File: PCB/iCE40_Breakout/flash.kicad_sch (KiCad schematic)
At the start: 47 parts, among them J4 prog_hdr, Q10 L2N7002SLLT1G, Q11 L2N7002SLLT1G, Q12 L2N7002SLLT1G, Q2 L2N7002SLLT1G, Q3 L2N7002SLLT1G, Q4 L2N7002SLLT1G, Q5 L2N7002SLLT1G, Q6 L2N7002SLLT1G, Q7 L2N7002SLLT1G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

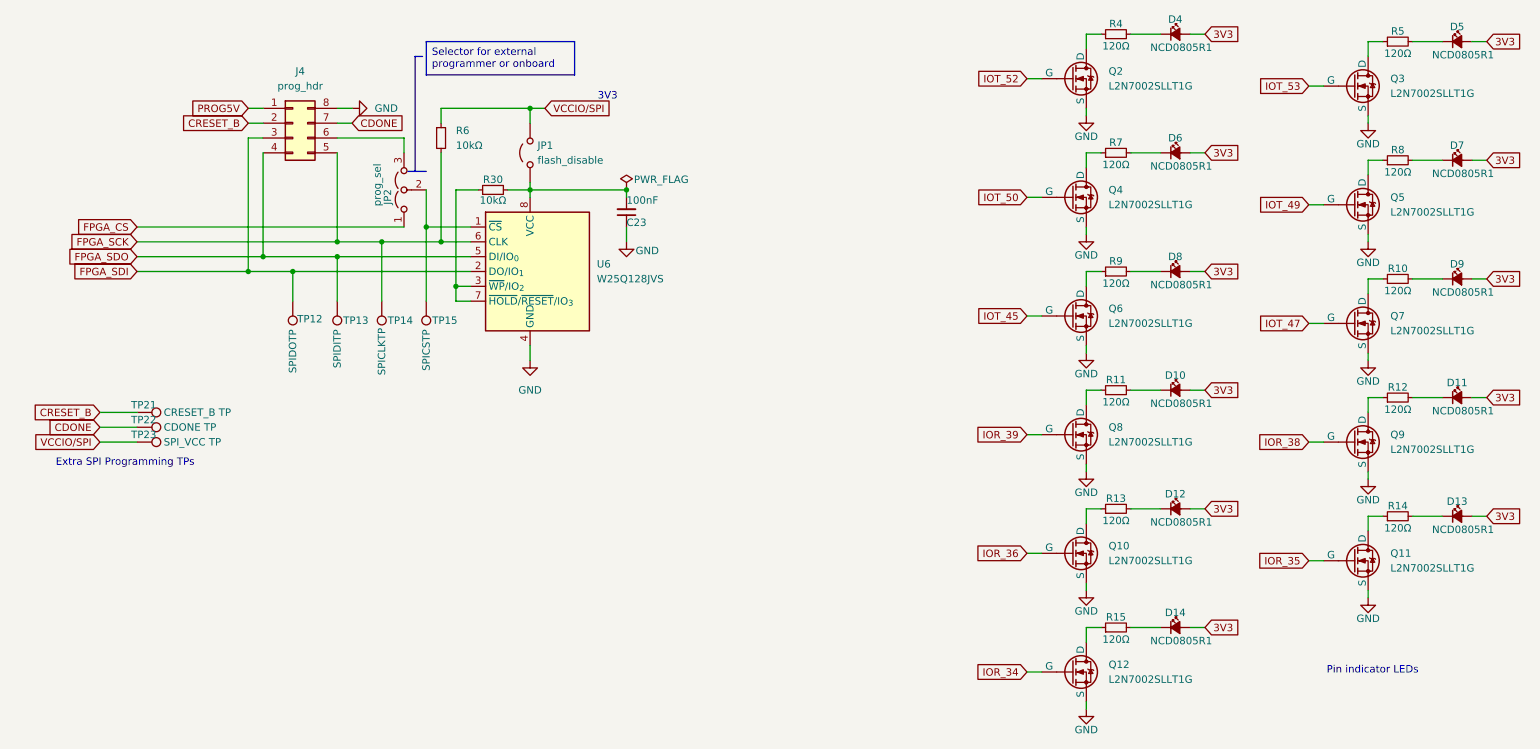
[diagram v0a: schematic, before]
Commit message: removed unecassary test points and excess LEDs
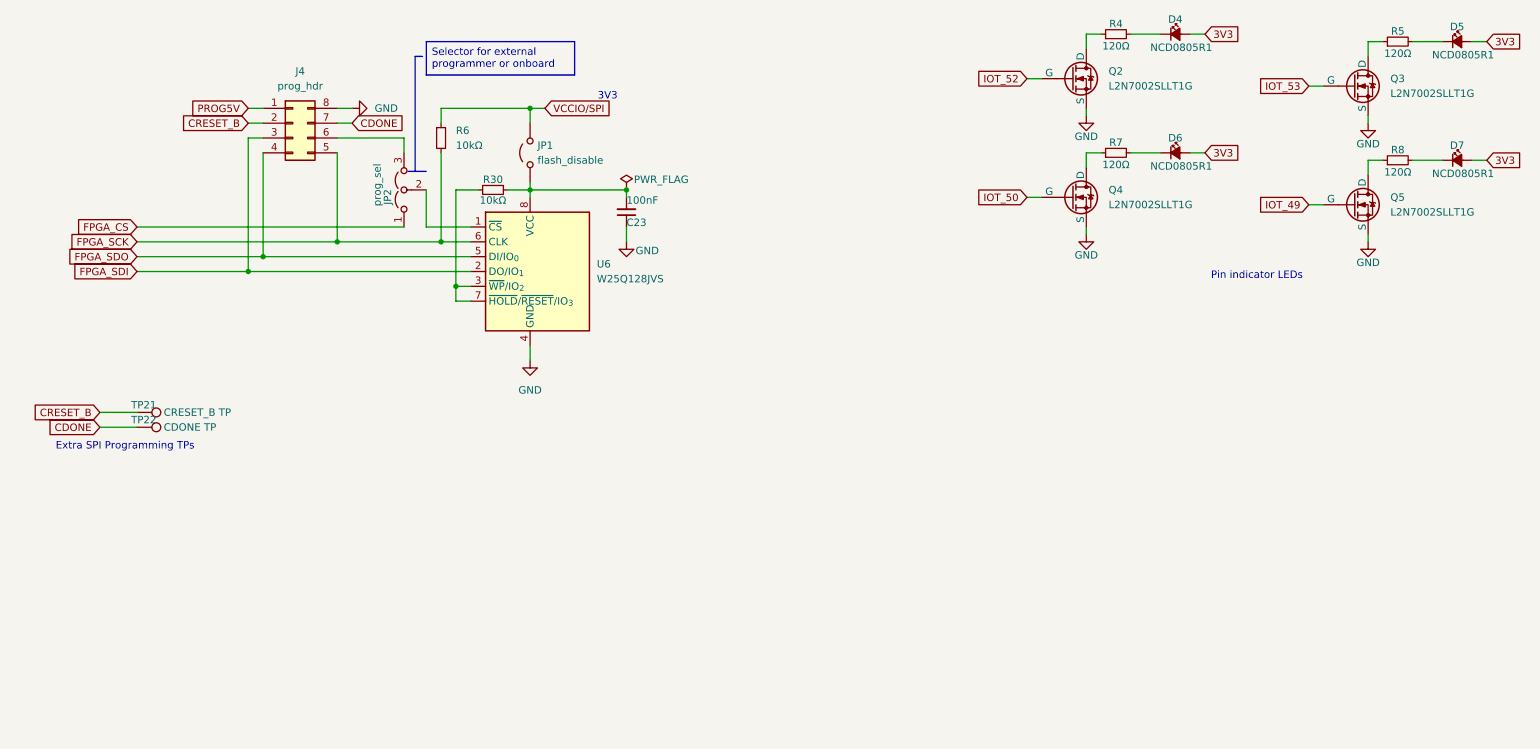
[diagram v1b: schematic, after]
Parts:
- removed D10, D11, D12, D13, D14, D8, D9: NCD0805R1, LED_SMD:LED_0805_2012Metric, symbol Device:LED_Small_Filled
- removed Q10, Q11, Q12, Q6, Q7, Q8, Q9: L2N7002SLLT1G, Package_TO_SOT_SMD:SOT-23, symbol Simulation_SPICE:NMOS
- removed R10, R11, R12, R13, R14, R15, R9: 120Ω, Resistor_SMD:R_0603_1608Metric, symbol Device:R_Small
- removed TP12: SPIDOTP, TestPoint:TestPoint_Pad_D1.0mm, symbol Connector:TestPoint
- removed TP13: SPIDITP, TestPoint:TestPoint_Pad_D1.0mm, symbol Connector:TestPoint
- removed TP14: SPICLKTP, TestPoint:TestPoint_Pad_D1.0mm, symbol Connector:TestPoint
- removed TP15: SPICSTP, TestPoint:TestPoint_Pad_D1.0mm, symbol Connector:TestPoint
- removed TP23: SPI_VCC TP, TestPoint:TestPoint_Pad_D1.0mm, symbol Connector:TestPoint

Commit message: Changed all pin sockets to be headers
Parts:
- JP2: footprint Connector_PinSocket_2.54mm:PinSocket_1x03_P2.54mm_Vertical -> Connector_PinHeader_2.54mm:PinHeader_1x03_P2.54mm_Vertical
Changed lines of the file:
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@@
 			)
 		)
-		(property "Footprint" "Connector_PinSocket_2.54mm:PinSocket_1x03_P2.54mm_Vertical"
+		(property "Footprint" "Connector_PinHeader_2.54mm:PinHeader_1x03_P2.54mm_Vertical"
 			(at 87.63 45.72 0)
 			(effects

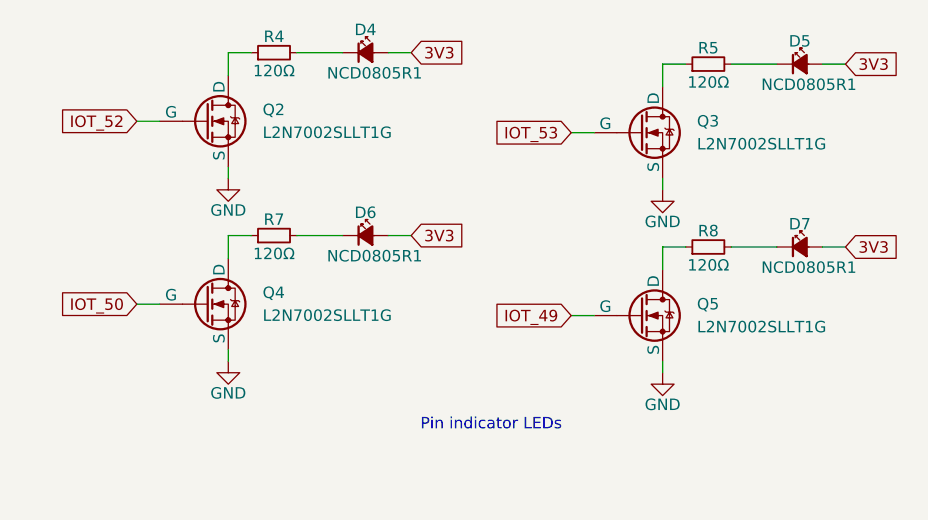
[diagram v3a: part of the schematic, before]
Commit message: Changed multiple caps, LEDs and NMOSs to JLCPCB basic parts
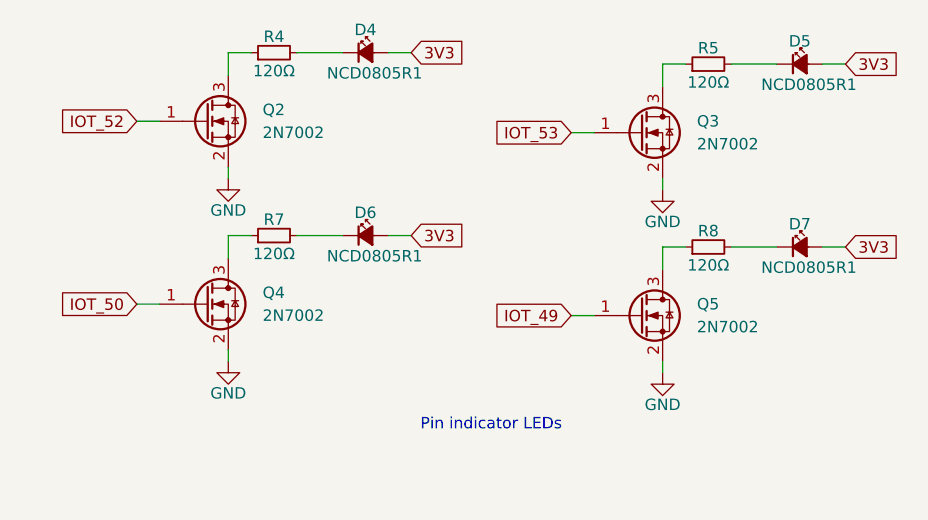
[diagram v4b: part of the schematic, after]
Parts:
- Q2, Q3, Q4, Q5: value L2N7002SLLT1G -> 2N7002; symbol Simulation_SPICE:NMOS -> Transistor_FET:2N7002; LCSC C22446827 -> C8545
- U6: LCSC C2613930 -> C97521
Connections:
- net GND: now also Q2.2 (S), Q3.2 (S), Q4.2 (S), Q5.2 (S); no longer Q2.3 (S), Q3.3 (S), Q4.3 (S), Q5.3 (S)
- net IOT_49: now also Q5.1 (G); no longer Q5.2 (G)
- net IOT_50: now also Q4.1 (G); no longer Q4.2 (G)
- net IOT_52: now also Q2.1 (G); no longer Q2.2 (G)
- net IOT_53: now also Q3.1 (G); no longer Q3.2 (G)
- net at R5.1: now also Q3.3 (D); no longer Q3.1 (D)
- net at R7.1: now also Q4.3 (D); no longer Q4.1 (D)
- net at R8.1: now also Q5.3 (D); no longer Q5.1 (D)
- net at R4.1: now also Q2.3 (D); no longer Q2.1 (D)
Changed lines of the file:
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@@
 			)
 		)
-		(property "LCSC" "C2613930"
+		(property "LCSC" "C97521"
 			(at 109.22 59.69 0)
 			(effects
@@
 	)
 	(symbol
-		(lib_id "Simulation_SPICE:NMOS")
+		(lib_id "Transistor_FET:2N7002")
 		(at 250.19 27.94 0)
 		(unit 1)
@@
 			)
 		)
-		(property "Value" "L2N7002SLLT1G"
+		(property "Value" "2N7002"
 			(at 256.54 29.21 0)
 			(effects
@@
 		)
 		(property "Footprint" "Package_TO_SOT_SMD:SOT-23"
-			(at 255.27 25.4 0)
-			(effects
-				(font
-					(size 1.27 1.27)
-				)
-				(hide yes)
-			)
-		)
-		(property "Datasheet" ""
-			(at 250.19 40.64 0)
-			(effects
-				(font
-					(size 1.27 1.27)
-				)
-				(hide yes)
-			)
-		)
-		(property "Description" "N-MOSFET transistor, drain/source/gate"
+			(at 255.27 29.845 0)
+			(effects
+				(font
+					(size 1.27 1.27)
+					(italic yes)
+				)
+				(justify left)
+				(hide yes)
+			)
+		)
+		(property "Datasheet" "https://www.onsemi.com/pub/Collateral/NDS7002A-D.PDF"
+			(at 255.27 31.75 0)
+			(effects
+				(font
+					(size 1.27 1.27)
+				)
+				(justify left)
+				(hide yes)
+			)
+		)
+		(property "Description" "0.115A Id, 60V Vds, N-Channel MOSFET, SOT-23"
 			(at 250.19 27.94 0)
 			(effects
@@
 			)
 		)
-		(property "LCSC" "C22446827"
+		(property "LCSC" "C8545"
 			(at 250.19 27.94 0)
 			(effects
@@
 	)
 	(symbol
-		(lib_id "Simulation_SPICE:NMOS")
+		(lib_id "Transistor_FET:2N7002")
 		(at 201.93 46.99 0)
 		(unit 1)
@@
 			)
 		)
-		(property "Value" "L2N7002SLLT1G"
+		(property "Value" "2N7002"
 			(at 208.28 48.26 0)
 			(effects
@@
 		)
 		(property "Footprint" "Package_TO_SOT_SMD:SOT-23"
-			(at 207.01 44.45 0)
-			(effects
-				(font
-					(size 1.27 1.27)
-				)
-				(hide yes)
-			)
-		)
-		(property "Datasheet" ""
-			(at 201.93 59.69 0)
-			(effects
-				(font
-					(size 1.27 1.27)
-				)
-				(hide yes)
-			)
-		)
-		(property "Description" "N-MOSFET transistor, drain/source/gate"
+			(at 207.01 48.895 0)
+			(effects
+				(font
+					(size 1.27 1.27)
+					(italic yes)
+				)
+				(justify left)
+				(hide yes)
+			)
+		)
+		(property "Datasheet" "https://www.onsemi.com/pub/Collateral/NDS7002A-D.PDF"
+			(at 207.01 50.8 0)
+			(effects
+				(font
+					(size 1.27 1.27)
+				)
+				(justify left)
+				(hide yes)
+			)
+		)
+		(property "Description" "0.115A Id, 60V Vds, N-Channel MOSFET, SOT-23"
 			(at 201.93 46.99 0)
 			(effects
@@
 			)
 		)
-		(property "LCSC" "C22446827"
+		(property "LCSC" "C8545"
 			(at 201.93 46.99 0)
 			(effects
@@
 	)
 	(symbol
-		(lib_id "Simulation_SPICE:NMOS")
+		(lib_id "Transistor_FET:2N7002")
 		(at 250.19 48.26 0)
 		(unit 1)
@@
 			)
 		)
-		(property "Value" "L2N7002SLLT1G"
+		(property "Value" "2N7002"
 			(at 256.54 49.53 0)
 			(effects
@@
 		)
 		(property "Footprint" "Package_TO_SOT_SMD:SOT-23"
-			(at 255.27 45.72 0)
-			(effects
-				(font
-					(size 1.27 1.27)
-				)
-				(hide yes)
-			)
-		)
-		(property "Datasheet" ""
-			(at 250.19 60.96 0)
-			(effects
-				(font
-					(size 1.27 1.27)
-				)
-				(hide yes)
-			)
-		)
-		(property "Description" "N-MOSFET transistor, drain/source/gate"
+			(at 255.27 50.165 0)
+			(effects
+				(font
+					(size 1.27 1.27)
+					(italic yes)
+				)
+				(justify left)
+				(hide yes)
+			)
+		)
+		(property "Datasheet" "https://www.onsemi.com/pub/Collateral/NDS7002A-D.PDF"
+			(at 255.27 52.07 0)
+			(effects
+				(font
+					(size 1.27 1.27)
+				)
+				(justify left)
+				(hide yes)
+			)
+		)
+		(property "Description" "0.115A Id, 60V Vds, N-Channel MOSFET, SOT-23"
 			(at 250.19 48.26 0)
 			(effects
@@
 			)
 		)
-		(property "LCSC" "C22446827"
+		(property "LCSC" "C8545"
 			(at 250.19 48.26 0)
 			(effects
@@
 	)
 	(symbol
-		(lib_id "Simulation_SPICE:NMOS")
+		(lib_id "Transistor_FET:2N7002")
 		(at 201.93 26.67 0)
 		(unit 1)
@@
 			)
 		)
-		(property "Value" "L2N7002SLLT1G"
+		(property "Value" "2N7002"
 			(at 208.28 27.94 0)
 			(effects
@@
 		)
 		(property "Footprint" "Package_TO_SOT_SMD:SOT-23"
-			(at 207.01 24.13 0)
-			(effects
-				(font
-					(size 1.27 1.27)
-				)
-				(hide yes)
-			)
-		)
-		(property "Datasheet" ""
-			(at 201.93 39.37 0)
-			(effects
-				(font
-					(size 1.27 1.27)
-				)
-				(hide yes)
-			)
-		)
-		(property "Description" "N-MOSFET transistor, drain/source/gate"
+			(at 207.01 28.575 0)
+			(effects
+				(font
+					(size 1.27 1.27)
+					(italic yes)
+				)
+				(justify left)
+				(hide yes)
+			)
+		)
+		(property "Datasheet" "https://www.onsemi.com/pub/Collateral/NDS7002A-D.PDF"
+			(at 207.01 30.48 0)
+			(effects
+				(font
+					(size 1.27 1.27)
+				)
+				(justify left)
+				(hide yes)
+			)
+		)
+		(property "Description" "0.115A Id, 60V Vds, N-Channel MOSFET, SOT-23"
 			(at 201.93 26.67 0)
 			(effects
@@
 			)
 		)
-		(property "LCSC" "C22446827"
+		(property "LCSC" "C8545"
 			(at 201.93 26.67 0)
 			(effects

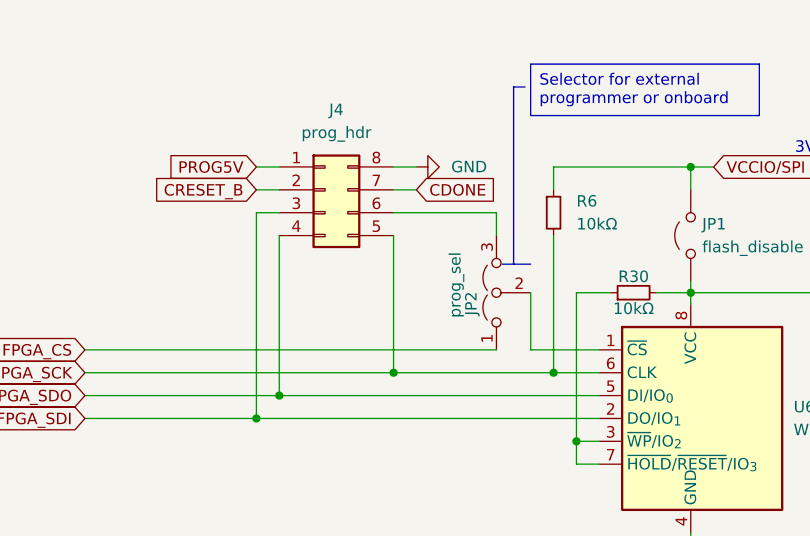
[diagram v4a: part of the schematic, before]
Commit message: Changed all manually placed components into DNP, and changed the manually added caps to 0603
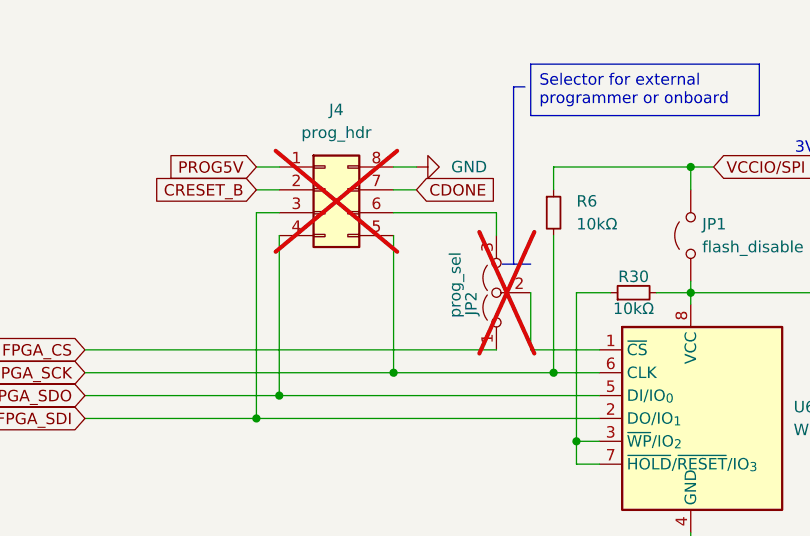
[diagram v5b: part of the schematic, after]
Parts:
- J4, JP2: now not fitted
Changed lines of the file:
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@@
 		(in_bom yes)
 		(on_board yes)
-		(dnp no)
+		(dnp yes)
 		(fields_autoplaced yes)
 		(property "Reference" "J4"
@@
 		(in_bom no)
 		(on_board yes)
-		(dnp no)
+		(dnp yes)
 		(property "Reference" "JP2"
 			(at 84.836 48.26 0)
